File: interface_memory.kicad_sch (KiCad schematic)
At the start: 52 parts, among them IC304 ?, IC509 M41464, IC510 M41464, IC512 LC3517BML, IC516 74LS244, IC517 74LS244, IC518 74LS244, IC519 74F32, IC520 74LS245, Q102 Q_NPN_CBE

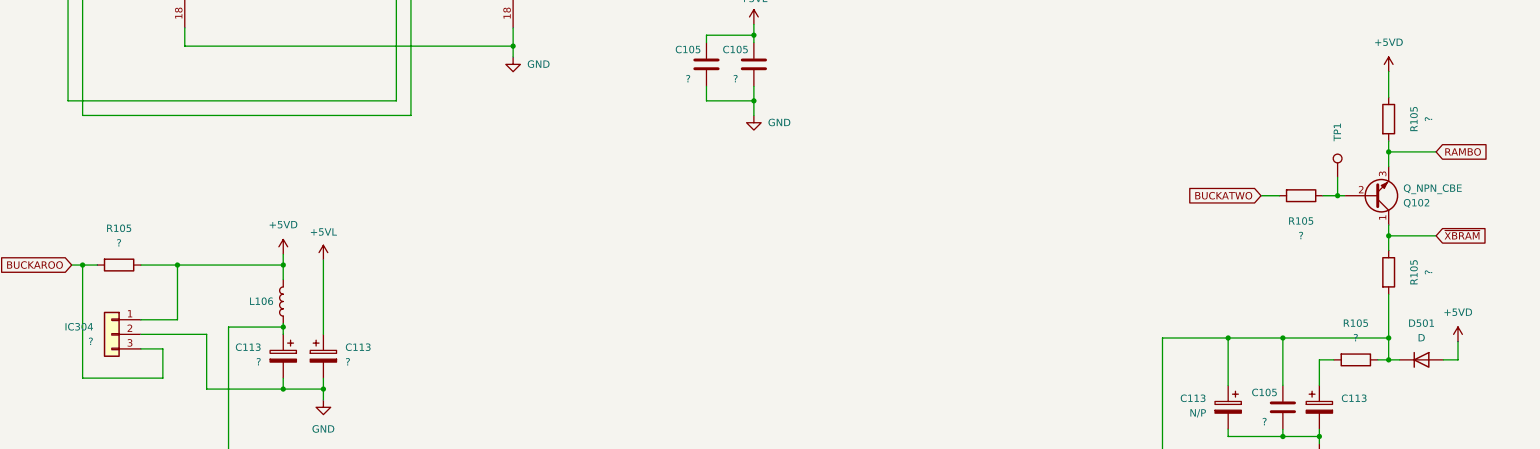
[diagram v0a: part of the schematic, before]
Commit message: Add resistor values to schematics.
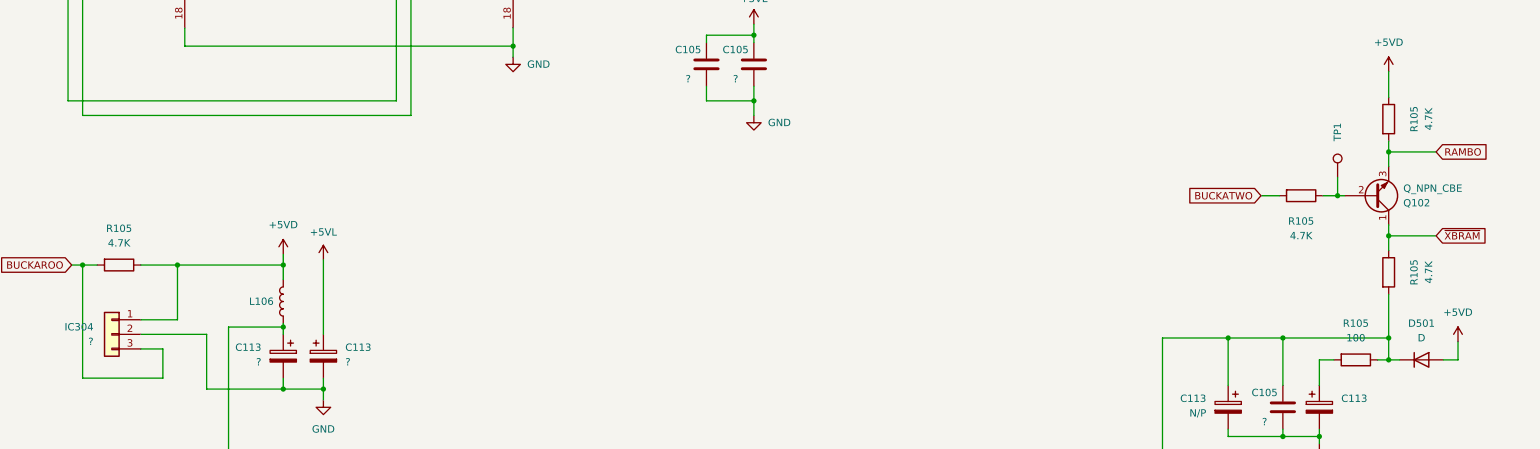
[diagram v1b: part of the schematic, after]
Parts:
- R105: value ? -> 4.7K
- R105: value ? -> 100
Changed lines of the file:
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@@
       (effects (font (size 1.27 1.27)))
     )
-    (property "Value" "?" (at 279.4 128.905 90)
+    (property "Value" "4.7K" (at 279.4 128.905 90)
       (effects (font (size 1.27 1.27)))
     )
@@
       (effects (font (size 1.27 1.27)))
     )
-    (property "Value" "?" (at 301.625 135.255 90)
+    (property "Value" "4.7K" (at 301.625 135.255 90)
       (effects (font (size 1.27 1.27)))
     )
@@
       (effects (font (size 1.27 1.27)))
     )
-    (property "Value" "?" (at 288.925 146.685 90)
+    (property "Value" "100" (at 288.925 146.685 90)
       (effects (font (size 1.27 1.27)))
     )
@@
       (effects (font (size 1.27 1.27)))
     )
-    (property "Value" "?" (at 301.625 108.585 90)
+    (property "Value" "4.7K" (at 301.625 108.585 90)
       (effects (font (size 1.27 1.27)))
     )
@@
       (effects (font (size 1.27 1.27)))
     )
-    (property "Value" "?" (at 73.66 130.175 90)
-      (effects (font (size 1.27 1.27)))
-    )
+    (property "Value" "4.7K" (at 73.66 130.175 90)
+      (effects (font (size 1.27 1.27)))
+    )

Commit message: Schematic clean-up.
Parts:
- IC304: symbol Connector_Generic:Conn_01x03 -> Device:Q_NPN_EBC
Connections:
- net BACKUP_VCC: now reaches C105.2, C113.1, D501.1 (K), IC512.24 (VCC), R105.1, R105.2
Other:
- moved on the sheet: C105, C113, D501, IC509, IC510, IC512, IC513, IC514, IC515, IC519A, IC519B, IC519C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

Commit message: Intermediate commit after renaming some nets.
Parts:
- C113: value ~ -> 0.047F 5.5V SUPERCAP
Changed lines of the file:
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@@
       (effects (font (size 1.27 1.27)) (justify left))
     )
-    (property "Value" "~" (at 267.97 262.001 0)
+    (property "Value" "0.047F 5.5V SUPERCAP" (at 267.97 262.001 0)
       (effects (font (size 1.27 1.27)) (justify left))
     )

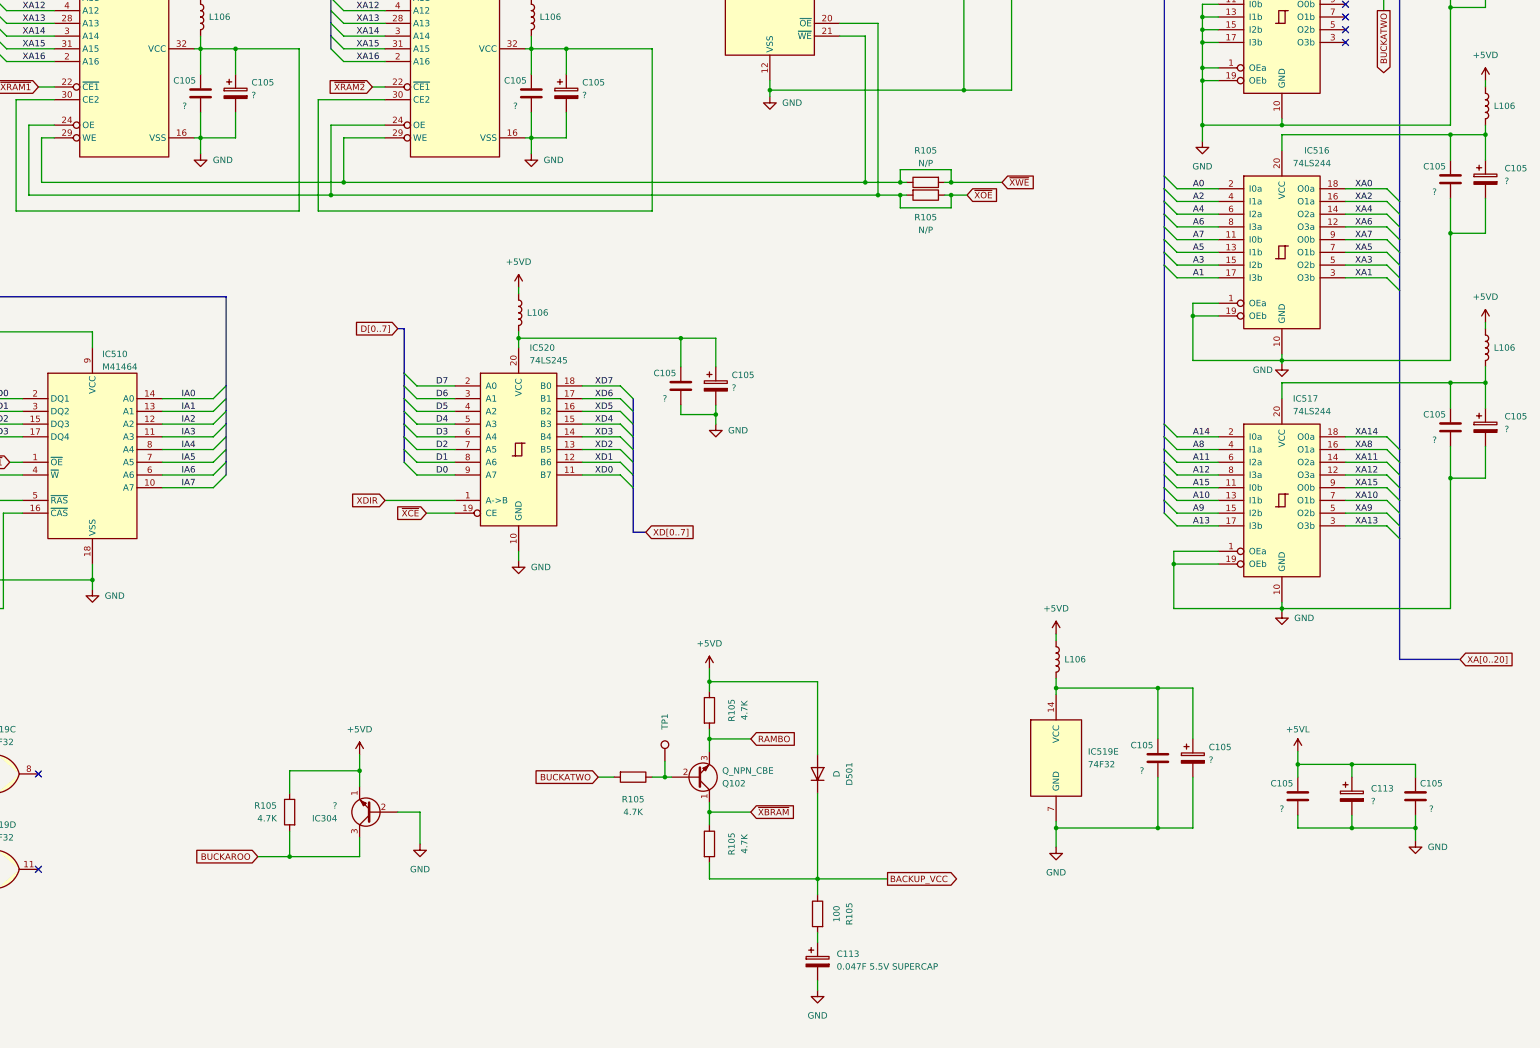
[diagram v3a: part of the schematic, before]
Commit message: Schematic clean-up (IFU ASIC and other stuff).
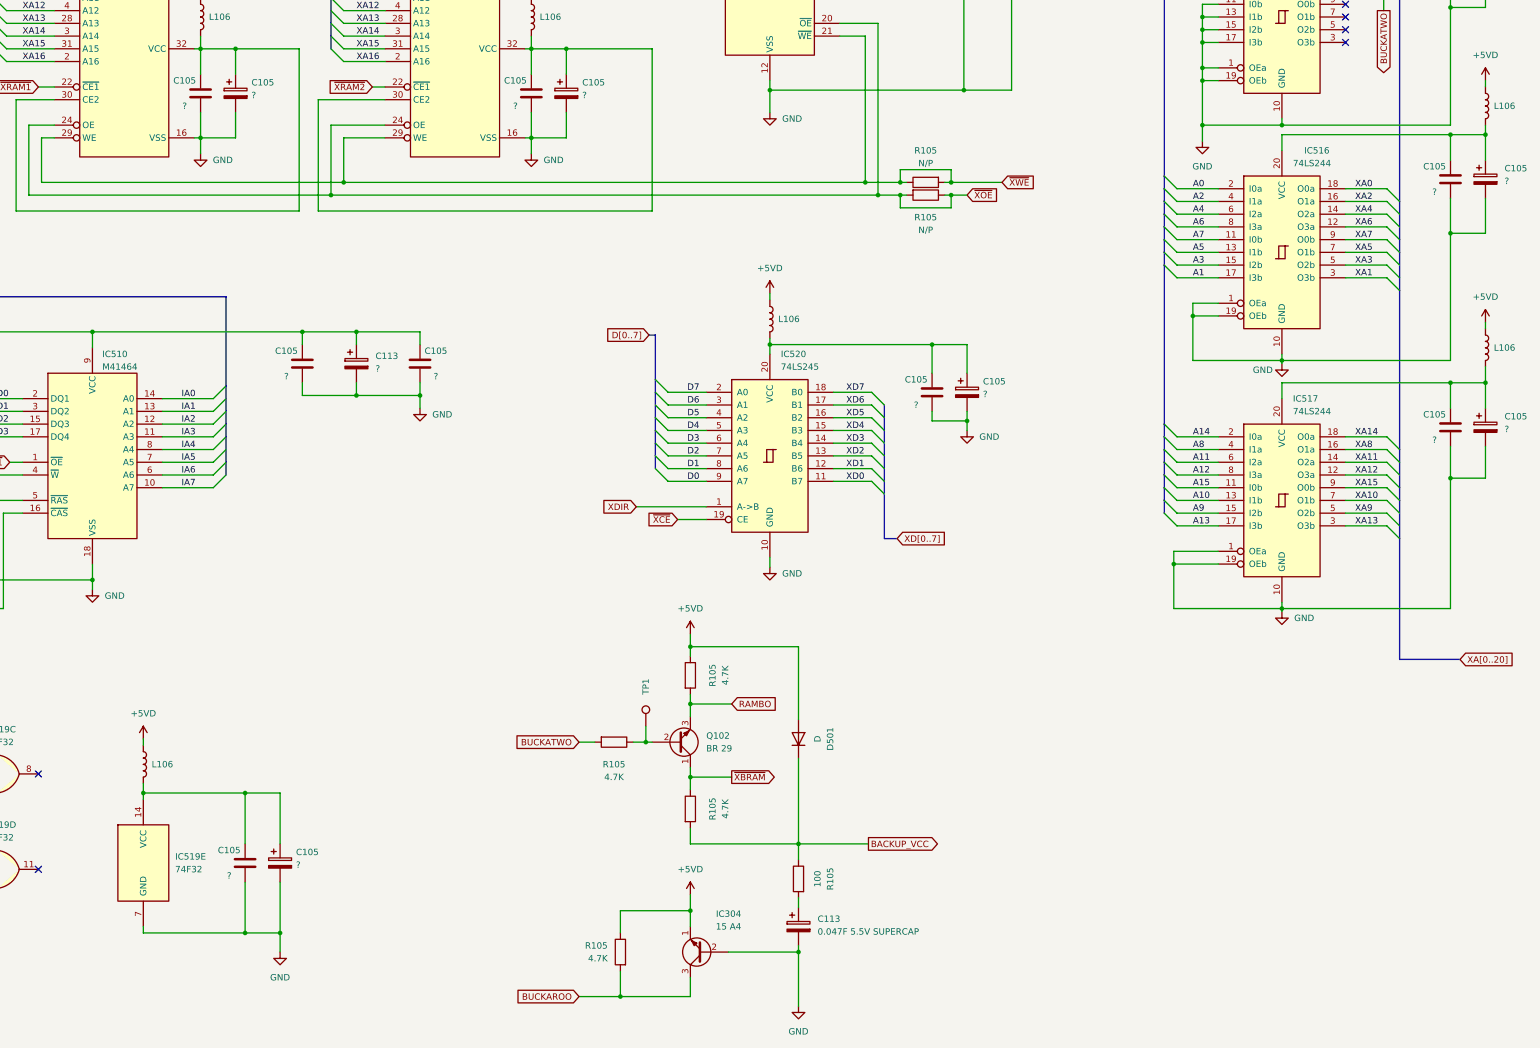
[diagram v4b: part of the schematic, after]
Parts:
- IC304: value ? -> 15 A4
- Q102: value Q_NPN_CBE -> BR 29
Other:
- moved on the sheet: C105, C113, D501, IC304, IC519E, IC520, L106, Q102, R105, TP1
